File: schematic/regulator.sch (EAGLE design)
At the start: 22 parts, among them J1 COMM, J2 STOP_LIGHT, Q1 NMOSFETSOT23, Q2 NMOSFETSOT23, Q3 NMOSFETSOT23, U1 MAX5035DIP8

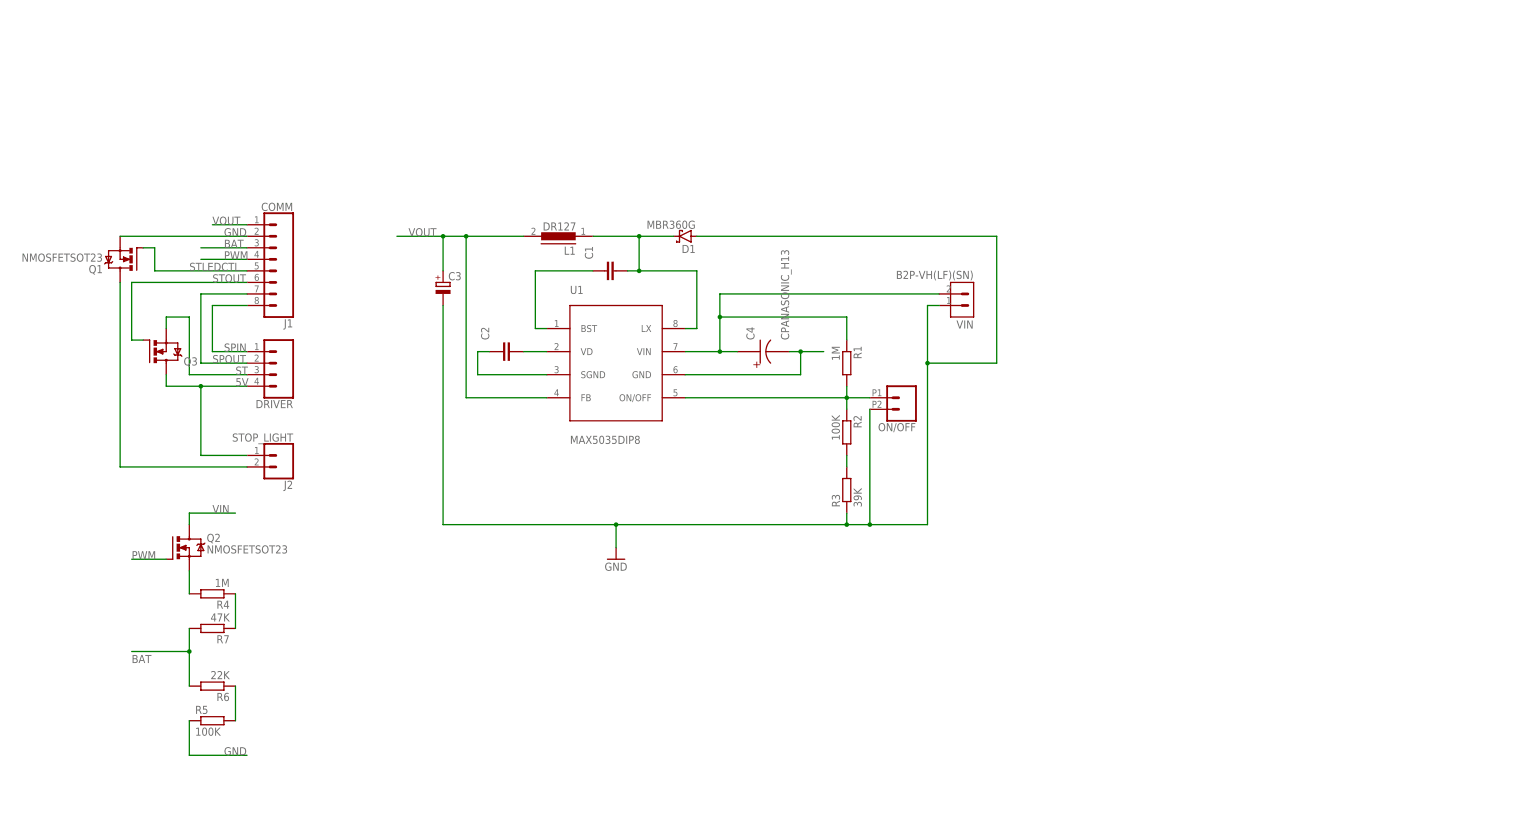
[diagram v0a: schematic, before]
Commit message: Update schematics
- Add TVS diodes for ESD protection
- Add resistors on MOSFET gates
- Make voltage divider on 2 resistors(4 previously)
- Align signal names on regulator and ECU schematics
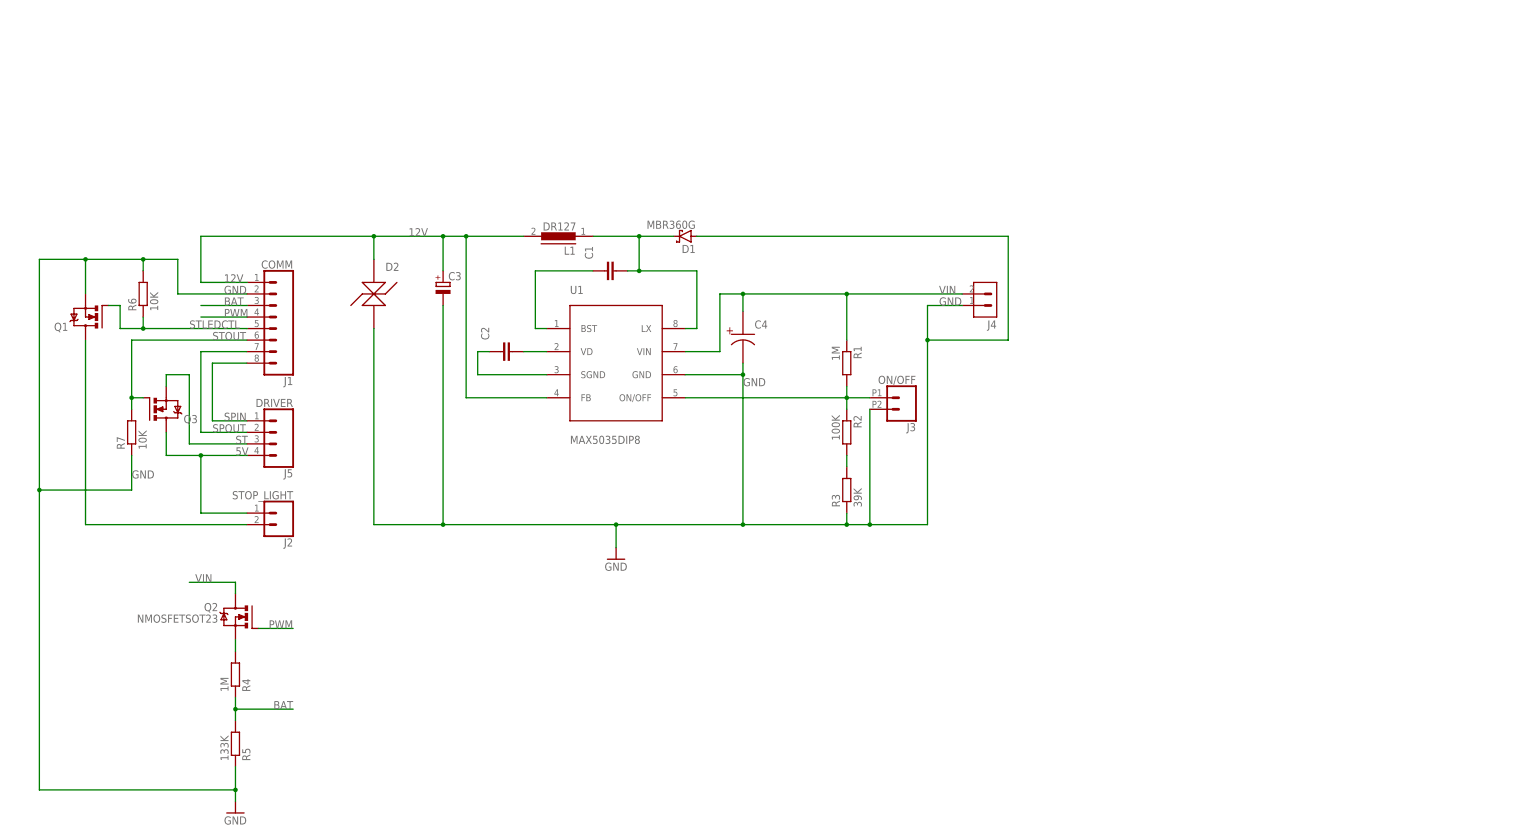
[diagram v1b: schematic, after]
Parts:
- removed DRIVER: (no value), SparkFun-Connectors:CONN_04
- removed VIN: B2P-VH(LF)(SN), Connectors:B2P-VH(LF)(SN)
- added D2: P4SMAJ12CA, eScooter:TVS_DIODESMA
- added J4: IN, Connectors:B2P-VH(LF)(SN)
- added J5: DRIVER, SparkFun-Connectors:CONN_04
- J3: value (none) -> ON/OFF
- R5: value 100K -> 133K
- R6: value 22K -> 10K
- R7: value 47K -> 10K
- renumbered ON/OFF to J3
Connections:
- removed net N$6: R4.1, R7.1
- removed net N$9: R5.2, R6.1
- removed net VOUT: C3.+, J1.1, L1.2, U1.FB
- new net 12V: C3.+, D2.P$1, J1.1, L1.2, U1.FB
- net 5V: now also J5.4; no longer DRIVER.4
- net BAT: now also R4.1, R5.2; no longer R6.2, R7.2
- net GND: now also D2.P$2, J4.1, R6.2, R7.1; no longer VIN.1
- net SPIN: now also J5.1; no longer DRIVER.1
- net SPOUT: now also J5.2; no longer DRIVER.2
- net ST: now also J5.3; no longer DRIVER.3
- net STLEDCTL: now also R6.1
- net STOUT: now also R7.2
- net VIN: now also J4.2; no longer VIN.2
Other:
- moved on the sheet: C4, J1, J2, Q1, Q2, Q3, R4, R5, R6, R7

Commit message: Update schematics for regulator
- Add elements nominals and correct values
- Fix library inconsistence
- Few cosmetical changes in schematics
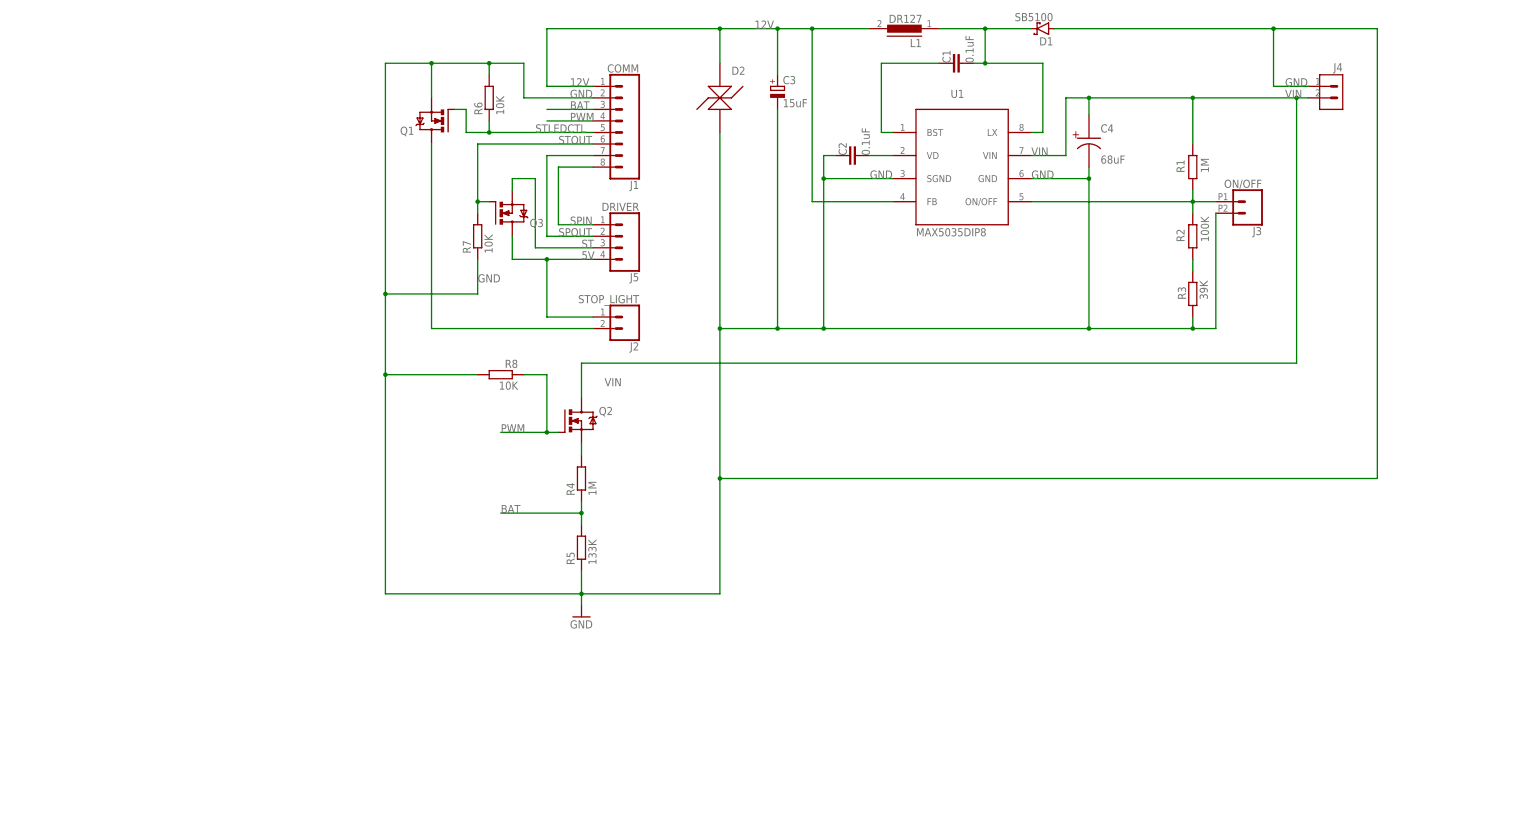
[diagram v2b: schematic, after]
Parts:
- added R8: 10K, eagle-ltspice:RR1206
- C1, C2: value (none) -> 0.1uF
- C3: value (none) -> 15uF
- C4: value CPANASONIC_H13 -> 68uF; device regulator:CPANASONIC_H13 -> eScooter:CPANASONIC_H13
- D1: value MBR360G -> SB5100
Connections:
- net GND: now also R8.2
- net PWM: now also R8.1
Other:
- moved on the sheet: C1, C2, C3, C4, D1, D2, J1, J2, J3, J4, J5, L1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

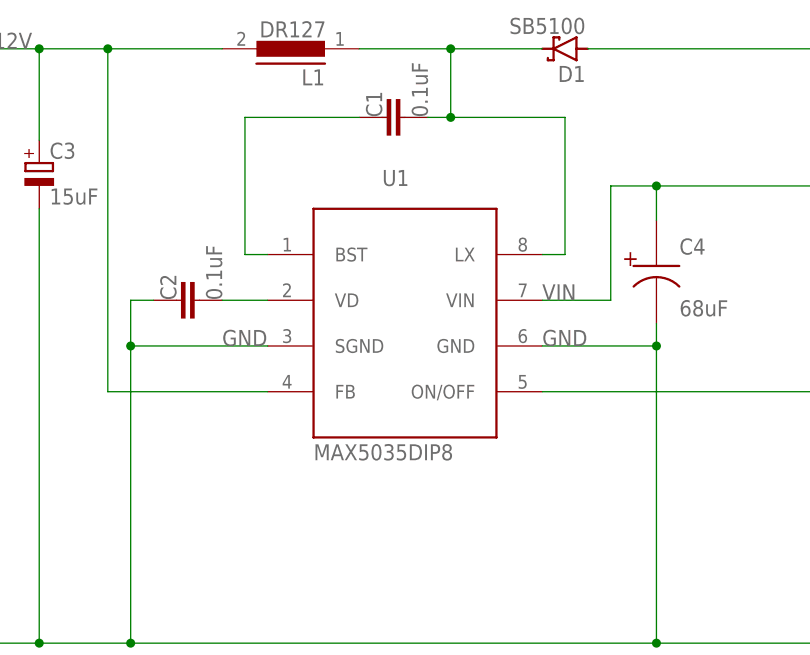
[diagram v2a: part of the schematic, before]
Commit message: Change MAX regulator package
- Change MAX package to drill-pin
- Move button to bottom layout
- Move elements for better work on regulator and ECU
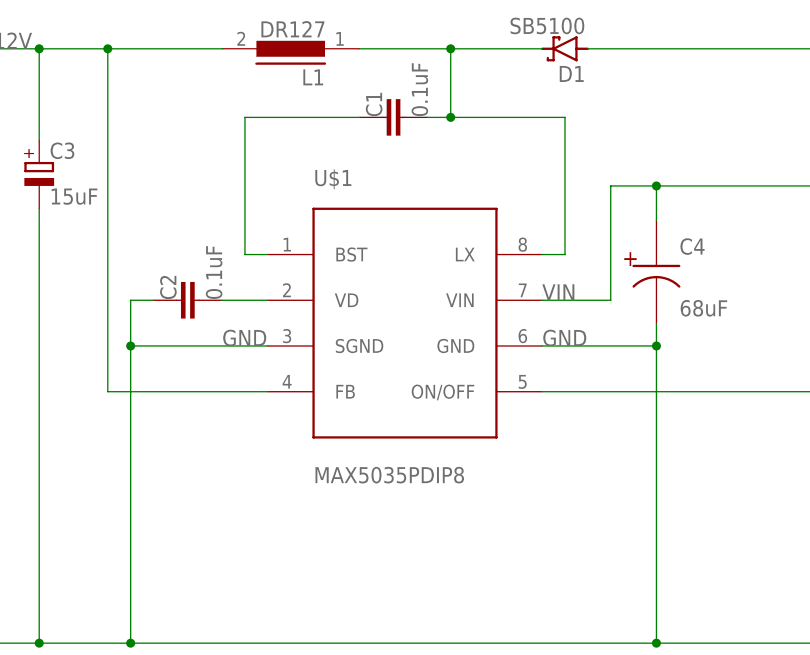
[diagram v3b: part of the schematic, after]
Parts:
- removed U1: MAX5035DIP8, regulator:MAX5035DIP8
- added U$1: MAX5035PDIP8, eScooter:MAX5035PDIP8
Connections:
- net 12V: now also U$1.FB; no longer U1.FB
- net GND: now also U$1.GND, U$1.SGND; no longer U1.GND, U1.SGND
- net N$1: now also U$1.BST; no longer U1.BST
- net N$2: now also U$1.LX; no longer U1.LX
- net N$4: now also U$1.VD; no longer U1.VD
- net N$5: now also U$1.ON/OFF; no longer U1.ON/OFF
- net VIN: now also U$1.VIN; no longer U1.VIN
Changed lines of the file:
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@@
 </classes>
 <parts>
-<part name="U1" library="regulator" deviceset="MAX5035" device="DIP8" package3d_urn="urn:adsk.eagle:package:8089856/1"/>
 <part name="J4" library="Connectors" library_urn="urn:adsk.eagle:library:14555660" deviceset="B2P-VH(LF)(SN)" device="" package3d_urn="urn:adsk.eagle:package:10989917/2" value="IN"/>
 <part name="C1" library="Capacitor" library_urn="urn:adsk.eagle:library:16290819" deviceset="C" device="CHIP-1206(3216-METRIC)" package3d_urn="urn:adsk.eagle:package:16290893/2" technology="_" value="0.1uF"/>
@@
 <part name="R8" library="eagle-ltspice" library_urn="urn:adsk.eagle:library:217" deviceset="R" device="R1206" package3d_urn="urn:adsk.eagle:package:13301/1" value="10K"/>
 <part name="C4" library="eScooter" deviceset="C" device="PANASONIC_H13" package3d_urn="urn:adsk.eagle:package:21812541/1" value="68uF"/>
+<part name="U$1" library="eScooter" deviceset="MAX5035" device="PDIP8" package3d_urn="urn:adsk.eagle:package:22059831/1"/>
 </parts>
 <sheets>
@@
 </plain>
 <instances>
-<instance part="U1" gate="G$1" x="132.08" y="101.6" smashed="yes">
-<attribute name="NAME" x="129.54" y="116.84" size="1.778" layer="95"/>
-<attribute name="VALUE" x="121.92" y="86.36" size="1.778" layer="96"/>
-</instance>
 <instance part="J4" gate="G$1" x="213.36" y="116.84" smashed="yes" rot="MR0">
 <attribute name="NAME" x="215.9" y="122.682" size="1.778" layer="95" rot="MR0"/>
@@
 <attribute name="NAME" x="162.56" y="109.22" size="1.778" layer="95"/>
 <attribute name="VALUE" x="162.56" y="104.14" size="1.778" layer="96" rot="MR180"/>
+</instance>
+<instance part="U$1" gate="G$1" x="132.08" y="101.6" smashed="yes">
+<attribute name="NAME" x="121.92" y="116.84" size="1.778" layer="95"/>
+<attribute name="VALUE" x="121.92" y="83.82" size="1.778" layer="96"/>
 </instance>
 </instances>
@@
 <pinref part="J3" gate="G$1" pin="2"/>
 <wire x1="187.96" y1="91.44" x2="187.96" y2="66.04" width="0.1524" layer="91"/>
-<pinref part="U1" gate="G$1" pin="GND"/>
 <wire x1="160.02" y1="99.06" x2="160.02" y2="101.6" width="0.1524" layer="91"/>
 <wire x1="147.32" y1="99.06" x2="160.02" y2="99.06" width="0.1524" layer="91"/>
@@
 <wire x1="223.52" y1="132.08" x2="223.52" y2="33.02" width="0.1524" layer="91"/>
 <wire x1="223.52" y1="33.02" x2="78.74" y2="33.02" width="0.1524" layer="91"/>
-<pinref part="U1" gate="G$1" pin="SGND"/>
 <wire x1="116.84" y1="99.06" x2="101.6" y2="99.06" width="0.1524" layer="91"/>
 <wire x1="101.6" y1="99.06" x2="101.6" y2="104.14" width="0.1524" layer="91"/>
@@
 <junction x="78.74" y="33.02"/>
 <pinref part="C4" gate="G$1" pin="P$2"/>
+<pinref part="U$1" gate="G$1" pin="SGND"/>
+<pinref part="U$1" gate="G$1" pin="GND"/>
 </segment>
 </net>
@@
 <wire x1="48.26" y1="50.8" x2="48.26" y2="58.42" width="0.1524" layer="91"/>
 <label x="53.34" y="53.34" size="1.778" layer="95"/>
-<pinref part="U1" gate="G$1" pin="VIN"/>
 <wire x1="147.32" y1="104.14" x2="154.94" y2="104.14" width="0.1524" layer="91"/>
 <wire x1="182.88" y1="116.84" x2="182.88" y2="106.68" width="0.1524" layer="91"/>
@@
 <pinref part="C4" gate="G$1" pin="P$1"/>
 <label x="147.32" y="104.14" size="1.778" layer="95"/>
+<pinref part="U$1" gate="G$1" pin="VIN"/>
 </segment>
 </net>
 <net name="N$1" class="0">
 <segment>
-<pinref part="U1" gate="G$1" pin="BST"/>
 <wire x1="116.84" y1="109.22" x2="114.3" y2="109.22" width="0.1524" layer="91"/>
 <wire x1="114.3" y1="109.22" x2="114.3" y2="124.46" width="0.1524" layer="91"/>
 <pinref part="C1" gate="G$1" pin="1"/>
 <wire x1="114.3" y1="124.46" x2="127" y2="124.46" width="0.1524" layer="91"/>
+<pinref part="U$1" gate="G$1" pin="BST"/>
 </segment>
 </net>
@@
 <wire x1="137.16" y1="124.46" x2="149.86" y2="124.46" width="0.1524" layer="91"/>
 <wire x1="149.86" y1="124.46" x2="149.86" y2="109.22" width="0.1524" layer="91"/>
-<pinref part="U1" gate="G$1" pin="LX"/>
 <wire x1="149.86" y1="109.22" x2="147.32" y2="109.22" width="0.1524" layer="91"/>
 <wire x1="137.16" y1="132.08" x2="137.16" y2="124.46" width="0.1524" layer="91"/>
@@
 <junction x="137.16" y="132.08"/>
 <pinref part="L1" gate="G$1" pin="1"/>
+<pinref part="U$1" gate="G$1" pin="LX"/>
 </segment>
 </net>
@@
 <wire x1="111.76" y1="132.08" x2="99.06" y2="132.08" width="0.1524" layer="91"/>
 <wire x1="99.06" y1="132.08" x2="99.06" y2="93.98" width="0.1524" layer="91"/>
-<pinref part="U1" gate="G$1" pin="FB"/>
 <wire x1="99.06" y1="93.98" x2="116.84" y2="93.98" width="0.1524" layer="91"/>
 <wire x1="99.06" y1="132.08" x2="91.44" y2="132.08" width="0.1524" layer="91"/>
@@
 <wire x1="78.74" y1="132.08" x2="78.74" y2="124.46" width="0.1524" layer="91"/>
 <junction x="78.74" y="132.08"/>
+<pinref part="U$1" gate="G$1" pin="FB"/>
 </segment>
 </net>
@@
 <segment>
 <pinref part="C2" gate="G$1" pin="2"/>
-<pinref part="U1" gate="G$1" pin="VD"/>
 <wire x1="111.76" y1="104.14" x2="116.84" y2="104.14" width="0.1524" layer="91"/>
+<pinref part="U$1" gate="G$1" pin="VD"/>
 </segment>
 </net>
 <net name="N$5" class="0">
 <segment>
-<pinref part="U1" gate="G$1" pin="ON/OFF"/>
 <wire x1="147.32" y1="93.98" x2="182.88" y2="93.98" width="0.1524" layer="91"/>
 <pinref part="R1" gate="G$1" pin="2"/>
@@
 <pinref part="J3" gate="G$1" pin="1"/>
 <wire x1="182.88" y1="93.98" x2="187.96" y2="93.98" width="0.1524" layer="91"/>
-</segment>
-</net>
+<pinref part="U$1" gate="G$1" pin="ON/OFF"/>
+</segment>
+</net>
